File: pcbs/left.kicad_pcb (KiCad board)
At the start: 2 copper layers, 121.1 x 91.2 mm, 27 parts

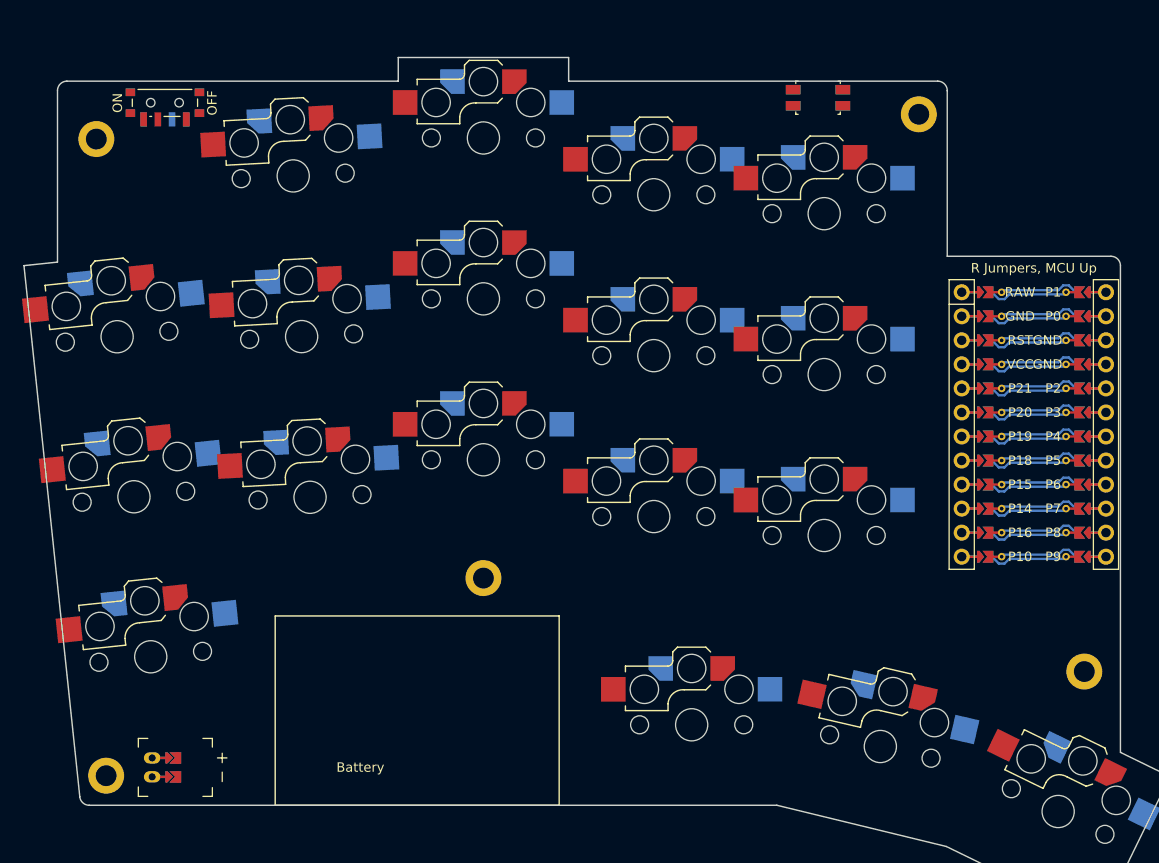
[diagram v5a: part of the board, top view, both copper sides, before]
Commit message: Convert most key-relative measures back to cpx/y
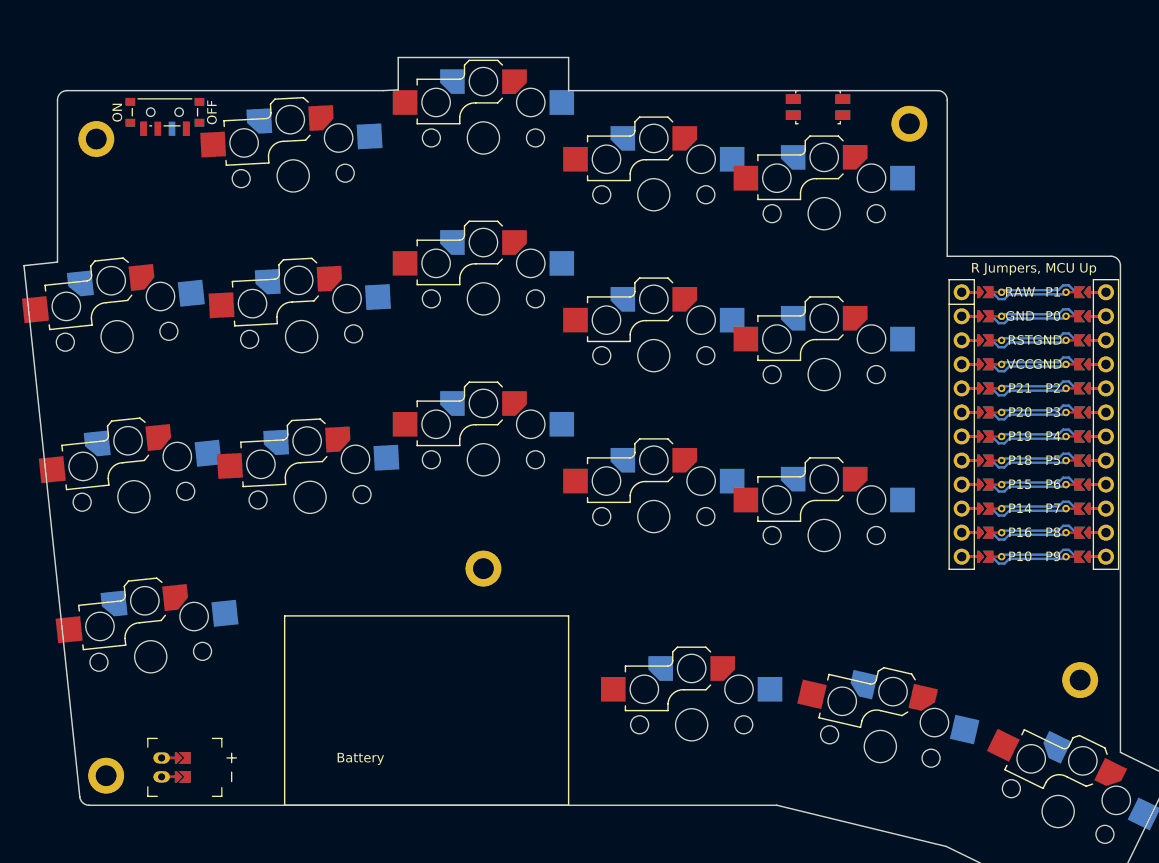
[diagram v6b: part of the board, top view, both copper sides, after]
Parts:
- moved H2 1.41 mm to (180.1, 43.7)
- moved H5 1.00 mm to (198.2, 102.5)
- moved H4 1.00 mm to (135.1, 90.7)
- moved JST1 1.00 mm to (101.1, 111.7)
- moved PWR1 1.00 mm to (101.5, 42.5)
- moved RST1 1.00 mm to (170.5, 41.9)
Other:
- outline, holes or cut-outs redrawn
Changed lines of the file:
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@@
   (footprint "ceoloide:power_switch_smd_side"
     (layer "F.Cu")
-    (at 101.49836669999999 41.48429119999999 90)
+    (at 101.49836669999999 42.48429119999999 90)
     (property "Reference" "PWR1"
       (at -3.6 0 0)
@@
   (footprint "ceoloide:reset_switch_smd_side"
     (layer "F.Cu")
-    (at 170.4983667 40.93429119999999 0)
+    (at 170.4983667 41.93429119999999 0)
     (property "Reference" "RST1"
       (at 0 0 0)
@@
     (footprint "ceoloide:battery_connector_jst_ph_2"
         (layer "F.Cu")
-        (at 100.1483666 111.68429119999999 90)
+        (at 101.1483666 111.68429119999999 90)
         (property "Reference" "JST1"
             (at 0 4.8 90)
@@
         )
     )
-    (segment (start 101.9483666 112.68429119999999) (end 100.1483666 112.68429119999999) (width 0.25) (layer "F.Cu") (net 53))
-    (segment (start 101.9483666 112.68429119999999) (end 100.1483666 112.68429119999999) (width 0.25) (layer "B.Cu") (net 53))
-    (segment (start 101.9483666 110.68429119999999) (end 100.1483666 110.68429119999999) (width 0.25) (layer "F.Cu") (net 54))
-    (segment (start 101.9483666 110.68429119999999) (end 100.1483666 110.68429119999999) (width 0.25) (layer "B.Cu") (net 54))
+    (segment (start 102.9483666 112.68429119999999) (end 101.1483666 112.68429119999999) (width 0.25) (layer "F.Cu") (net 53))
+    (segment (start 102.9483666 112.68429119999999) (end 101.1483666 112.68429119999999) (width 0.25) (layer "B.Cu") (net 53))
+    (segment (start 102.9483666 110.68429119999999) (end 101.1483666 110.68429119999999) (width 0.25) (layer "F.Cu") (net 54))
+    (segment (start 102.9483666 110.68429119999999) (end 101.1483666 110.68429119999999) (width 0.25) (layer "B.Cu") (net 54))
   (gr_text "Battery"
-    (at 122.1483666 111.68429119999999 0)
+    (at 122.1483666 110.68429119999999 0)
     (layer "F.SilkS" )
     (effects
@@
   (footprint "ceoloide:mounting_hole_plated"
     (layer "F.Cu")
-    (at 181.1483666 42.684291099999996 0)
+    (at 180.1483666 43.684291099999996 0)
     (property "Reference" "H2"
       (at 0 3 0)
@@
   (footprint "ceoloide:mounting_hole_plated"
     (layer "F.Cu")
-    (at 135.1483667 91.68429119999999 0)
+    (at 135.1483667 90.68429119999999 0)
     (property "Reference" "H4"
       (at 0 3 0)
@@
   (footprint "ceoloide:mounting_hole_plated"
     (layer "F.Cu")
-    (at 198.6292952 101.55924569999999 -26)
+    (at 198.19092410000002 102.4580398 -26)
     (property "Reference" "H5"
       (at 0 3 -26)
@@
   (gr_line (start 86.60684319999999 58.67357570000001) (end 92.50479308505149 114.78881969999998) (layer Edge.Cuts) (stroke (width 0.15) (type default)))
 (gr_line (start 86.60684319999999 58.67357570000001) (end 90.1483667 58.30134658019551) (layer Edge.Cuts) (stroke (width 0.15) (type default)))
-(gr_line (start 144.1483666 39.18429119999999) (end 144.1483667 36.68429119999999) (layer Edge.Cuts) (stroke (width 0.15) (type default)))
+(gr_line (start 124.57345505196682 40.18429119999999) (end 126.1483667 40.10175357892617) (layer Edge.Cuts) (stroke (width 0.15) (type default)))
+(gr_line (start 144.1483666 40.18429119999999) (end 144.1483667 36.68429119999999) (layer Edge.Cuts) (stroke (width 0.15) (type default)))
 (gr_line (start 144.1483667 36.68429119999999) (end 126.1483667 36.68429119999999) (layer Edge.Cuts) (stroke (width 0.15) (type default)))
-(gr_line (start 126.1483667 36.68429119999999) (end 126.1483667 39.18429119999999) (layer Edge.Cuts) (stroke (width 0.15) (type default)))
+(gr_line (start 126.1483667 36.68429119999999) (end 126.1483667 40.10175357892617) (layer Edge.Cuts) (stroke (width 0.15) (type default)))
 (gr_line (start 93.49931498505148 115.68429119999999) (end 166.1483666 115.68429119999999) (layer Edge.Cuts) (stroke (width 0.15) (type default)))
 (gr_line (start 184.0527886 120.0396531) (end 200.23108150000002 127.93033369999999) (layer Edge.Cuts) (stroke (width 0.15) (type default)))
@@
 (gr_arc (start 202.4483666 58.684291099999996) (mid 202.1554734 57.9771843) (end 201.4483666 57.684291099999996) (layer Edge.Cuts) (stroke (width 0.15) (type default)))
 (gr_arc (start 92.50479308505149 114.78881969999996) (mid 92.83018438505148 115.42743599999996) (end 93.49931498505148 115.68429119999996) (layer Edge.Cuts) (stroke (width 0.15) (type default)))
-(gr_line (start 90.1483667 58.30134658019551) (end 90.1483667 40.18429119999999) (layer Edge.Cuts) (stroke (width 0.15) (type default)))
-(gr_line (start 91.1483667 39.18429119999999) (end 126.1483667 39.18429119999999) (layer Edge.Cuts) (stroke (width 0.15) (type default)))
-(gr_line (start 144.1483666 39.18429119999999) (end 183.1483667 39.18429119999999) (layer Edge.Cuts) (stroke (width 0.15) (type default)))
-(gr_line (start 184.1483667 40.18429119999999) (end 184.1483667 57.684291099999996) (layer Edge.Cuts) (stroke (width 0.15) (type default)))
-(gr_arc (start 91.1483667 39.18429119999999) (mid 90.44125989999999 39.47718439999999) (end 90.1483667 40.18429119999999) (layer Edge.Cuts) (stroke (width 0.15) (type default)))
-(gr_arc (start 184.1483667 40.18429119999999) (mid 183.8554735 39.47718439999999) (end 183.1483667 39.18429119999999) (layer Edge.Cuts) (stroke (width 0.15) (type default)))
-(gr_line (start 113.1483666 95.68429119999999) (end 113.1483666 115.68429119999999) (layer F.SilkS) (stroke (width 0.15) (type default)))
-(gr_line (start 113.1483666 115.68429119999999) (end 143.1483666 115.68429119999999) (layer F.SilkS) (stroke (width 0.15) (type default)))
-(gr_line (start 143.1483666 115.68429119999999) (end 143.1483666 95.68429119999999) (layer F.SilkS) (stroke (width 0.15) (type default)))
-(gr_line (start 143.1483666 95.68429119999999) (end 113.1483666 95.68429119999999) (layer F.SilkS) (stroke (width 0.15) (type default)))
+(gr_line (start 90.1483667 58.30134658019551) (end 90.1483667 41.18429119999999) (layer Edge.Cuts) (stroke (width 0.15) (type default)))
+(gr_line (start 91.1483667 40.18429119999999) (end 124.57345505196682 40.18429119999999) (layer Edge.Cuts) (stroke (width 0.15) (type default)))
+(gr_line (start 144.1483666 40.18429119999999) (end 183.1483667 40.18429119999999) (layer Edge.Cuts) (stroke (width 0.15) (type default)))
+(gr_line (start 184.1483667 41.18429119999999) (end 184.1483667 57.684291099999996) (layer Edge.Cuts) (stroke (width 0.15) (type default)))
+(gr_arc (start 91.1483667 40.18429119999999) (mid 90.44125989999999 40.47718439999999) (end 90.1483667 41.18429119999999) (layer Edge.Cuts) (stroke (width 0.15) (type default)))
+(gr_arc (start 184.1483667 41.18429119999999) (mid 183.8554735 40.47718439999999) (end 183.1483667 40.18429119999999) (layer Edge.Cuts) (stroke (width 0.15) (type default)))
+(gr_line (start 114.1483666 95.68429119999999) (end 114.1483666 115.68429119999999) (layer F.SilkS) (stroke (width 0.15) (type default)))
+(gr_line (start 114.1483666 115.68429119999999) (end 144.1483666 115.68429119999999) (layer F.SilkS) (stroke (width 0.15) (type default)))
+(gr_line (start 144.1483666 115.68429119999999) (end 144.1483666 95.68429119999999) (layer F.SilkS) (stroke (width 0.15) (type default)))
+(gr_line (start 144.1483666 95.68429119999999) (end 114.1483666 95.68429119999999) (layer F.SilkS) (stroke (width 0.15) (type default)))
 )
